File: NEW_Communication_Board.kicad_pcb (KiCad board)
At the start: 4 copper layers, 103.2 x 58.9 mm, 72 parts, among them J1 USB_IN, J2 IMU, J3 Mini Fuse Socket, J4 XM_conn, J5 HUB-3, J6 HUB-4, U1 FE1.1s, U2 FT232RL, U3 FT232RL, U5 FT232RL, U6 FT232RL, U7 AMS1117, U8 ST485E, Y1 Crystal 12MHz - ECS

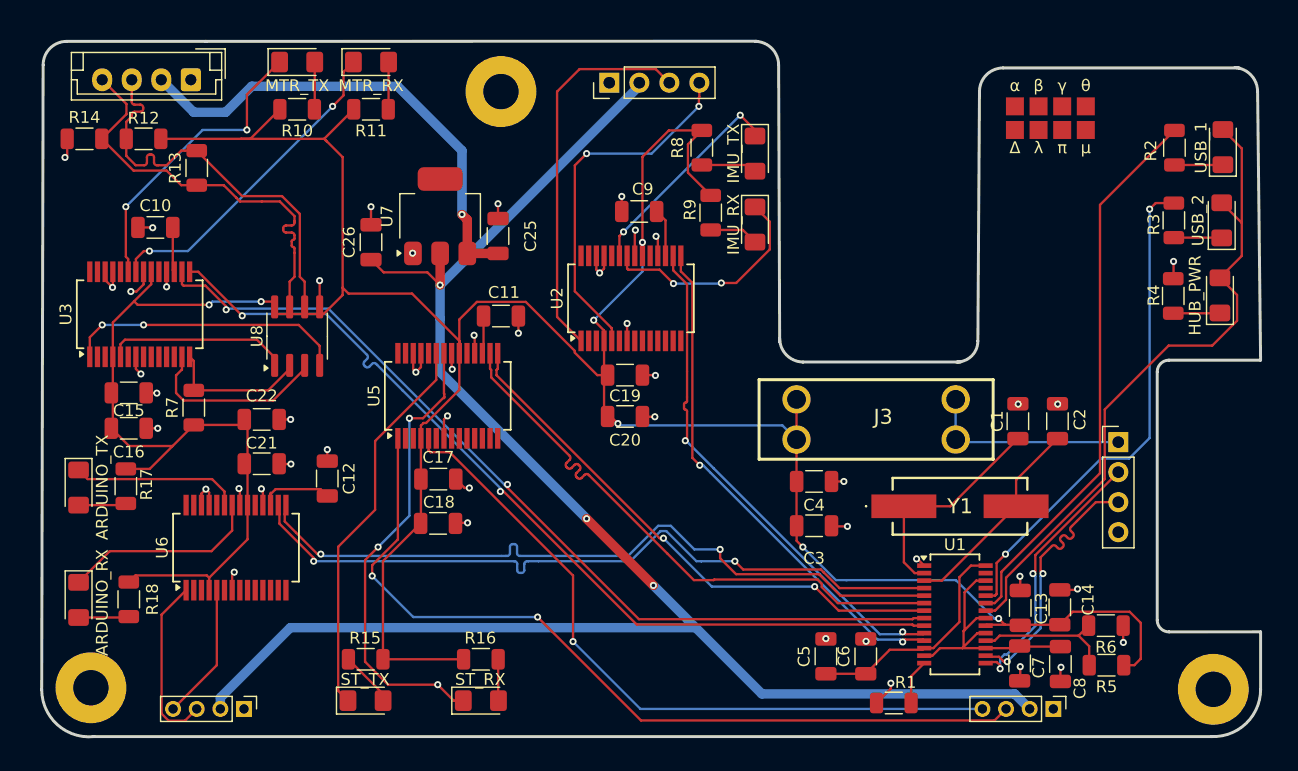
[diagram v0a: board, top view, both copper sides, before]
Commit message: Changing the LDO, and correcting the Edge.Cuts
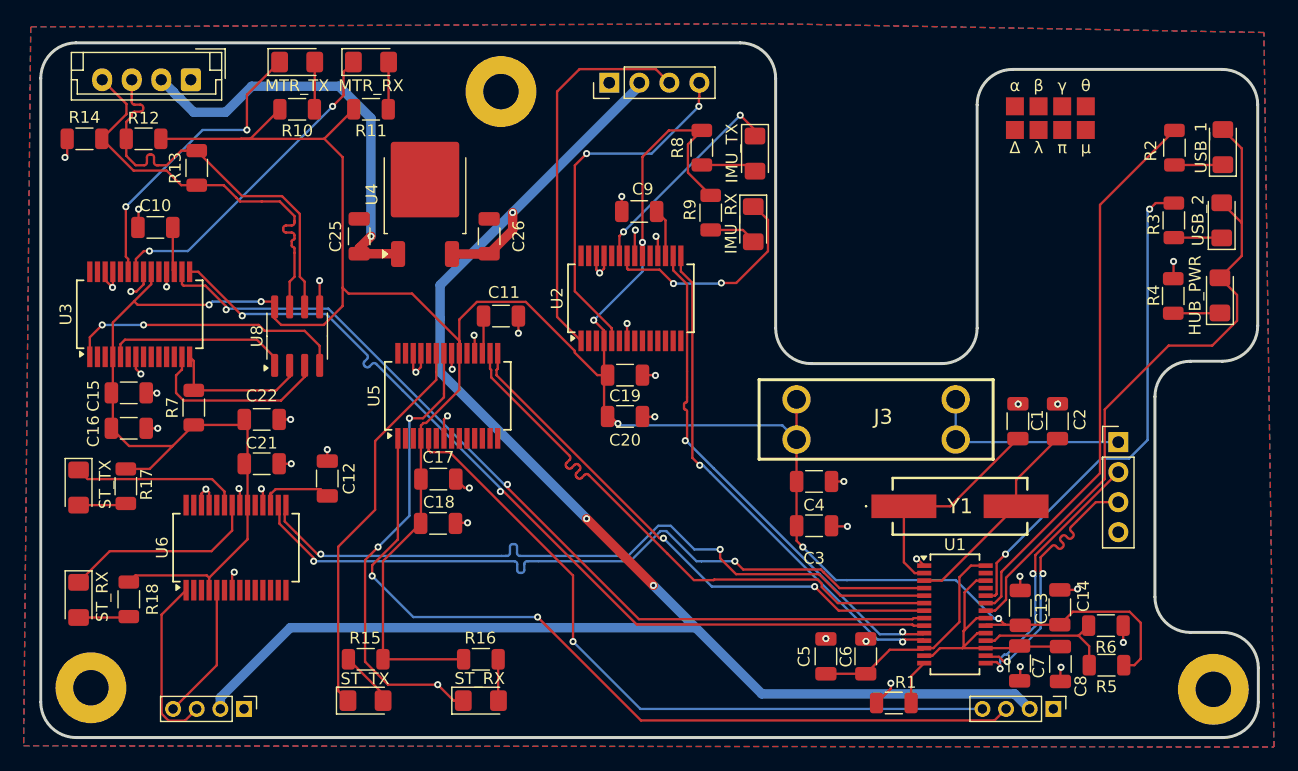
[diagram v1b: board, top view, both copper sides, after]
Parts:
- removed U7: AMS1117, Package_TO_SOT_SMD:SOT-223
- added U4: L7805, Package_TO_SOT_SMD:TO-252-2, F.Cu at (129.6, 61.0)
- D10: value ARDUINO_TX -> ST_TX
- D11: value ARDUINO_RX -> ST_RX
- moved C25 11.8 mm to (124.0, 64.5)
- moved C26 10.0 mm to (135.0, 64.5)
- moved D5 0.15 mm to (157.3, 63.5)
- turned C21 to 180 degrees
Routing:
- net Net-(J4-VDD): track 40.8 -> 36.1 mm
- net 5V: track 146.2 -> 144.3 mm
- net GNDREF: track 65.0 -> 63.6 mm, vias 46 -> 44
- net USB_PWR: track 284.8 -> 285.7 mm, vias 8 -> 7
- added copper zone on B.Cu, net GNDREF
- added copper zone on F.Cu, net GNDREF
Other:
- board size 103.2 x 58.9 mm -> 103 x 58.8 mm
